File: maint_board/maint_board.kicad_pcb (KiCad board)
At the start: 2 copper layers, 151.1 x 90.1 mm, 96 parts, among them J1 USB_mini_micro_B, J2 4P4C, J3 TC2030-IDC_FB, K1 KEYSW, K10 KEYSW, K11 KEYSW, K12 KEYSW, K13 KEYSW, K15 KEYSW, K16 KEYSW, K17 KEYSW, K18 KEYSW, K19 KEYSW, K2 KEYSW, K20 KEYSW, K29 KEYSW, K3 KEYSW, K30 KEYSW, K31 KEYSW, K4 KEYSW, K5 KEYSW, K6 KEYSW, K8 KEYSW, K9 KEYSW, Q1 Q_NMOS_GSD, SW1 SW_PUSH, U1 ATMEGA32U4, X1 XTAL_GND

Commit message: commit before reinstall computer
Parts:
- removed G***: LOGO, grafic:qr
- removed G***: LOGO, grafic:loggo2
- removed REF**: OSHW-Logo2_7.3x6mm_SilkScreen, Symbol:OSHW-Logo2_7.3x6mm_SilkScreen
- removed REF** (x3): MountingHole_2.2mm_M2, MountingHole:MountingHole_2.2mm_M2
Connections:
- R1 pad 2: Net-(R1-Pad2) -> rst_prog
- SW1 pad 2: Net-(R1-Pad2) -> rst_prog
- U1 pad 12: rst_prog -> (no net)
- U1 pad 13: Net-(R1-Pad2) -> rst_prog
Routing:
- net rst_prog: track 18.9 -> 61.6 mm, vias 0 -> 1
- net Net-(R1-Pad2): track 41.1 -> 0.00 mm, vias 1 -> 0

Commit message: updated submodule
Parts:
- K1, K10, K11, K12, K13, K15, K16, K17, K18, K19, K2, K20, K29, K3, K30, K31, K4, K5, K6, K8, K9: footprint keyswitches:SW_MX_reversible -> switches:SW_MX_reversible
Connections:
- D41 pad 4: (no net) -> Net-(D41-Pad4)
- D42 pad 4: (no net) -> Net-(D42-Pad4)
- D43 pad 1: (no net) -> Net-(D43-Pad1)
- D43 pad 6: (no net) -> Net-(D43-Pad6)
- D44 pad 3: (no net) -> Net-(D44-Pad3)
- D44 pad 4: (no net) -> Net-(D44-Pad4)
- J1 pad 4: (no net) -> Net-(J1-Pad4)
- U1 pad 1: (no net) -> Net-(U1-Pad1)
- U1 pad 12: (no net) -> Net-(U1-Pad12)
- U1 pad 20: (no net) -> Net-(U1-Pad20)
- U1 pad 25: (no net) -> Net-(U1-Pad25)
- U1 pad 26: (no net) -> Net-(U1-Pad26)
- U1 pad 36: (no net) -> Net-(U1-Pad36)
- U1 pad 42: (no net) -> Net-(U1-Pad42)
- U1 pad 7: (no net) -> Net-(U1-Pad7)
- U1 pad 8: (no net) -> Net-(U1-Pad8)

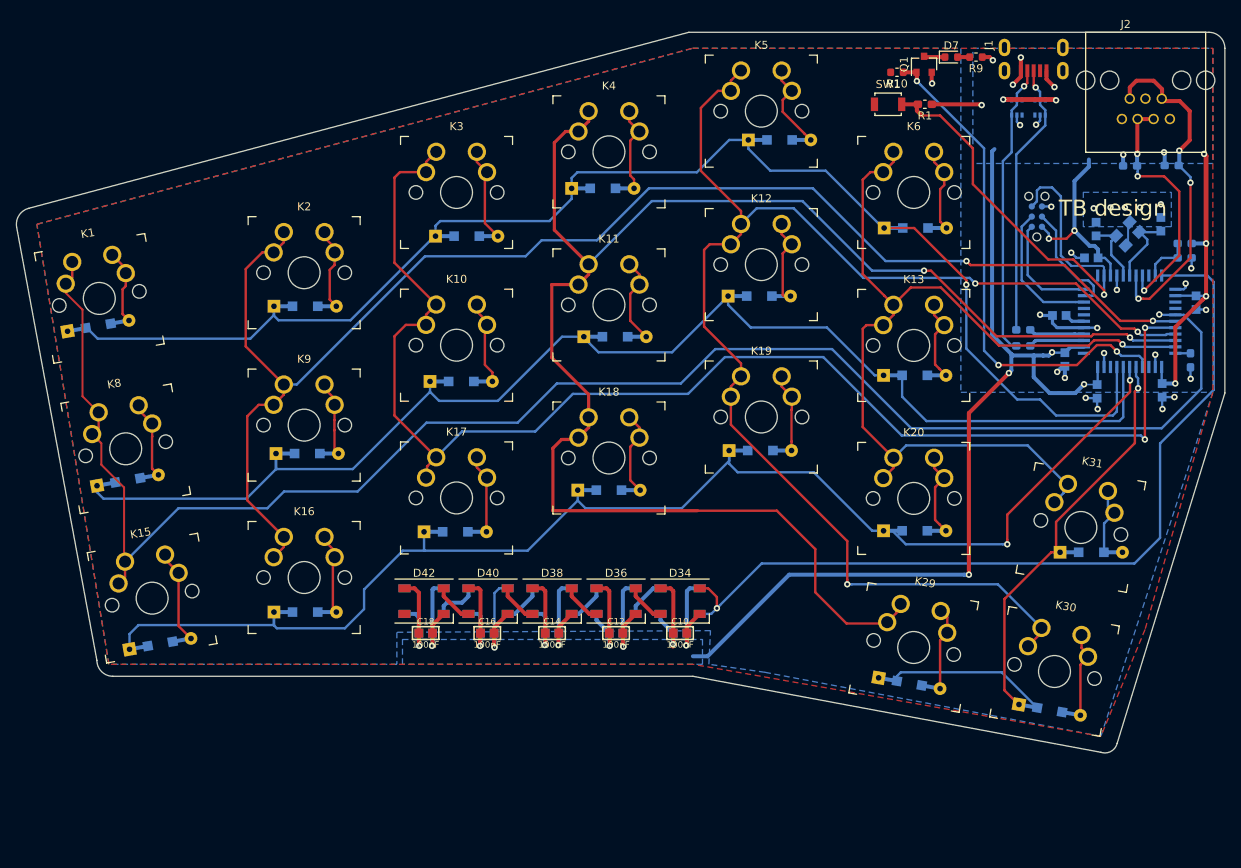
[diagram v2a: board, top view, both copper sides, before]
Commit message: removed two leds and fixed recet and usb port
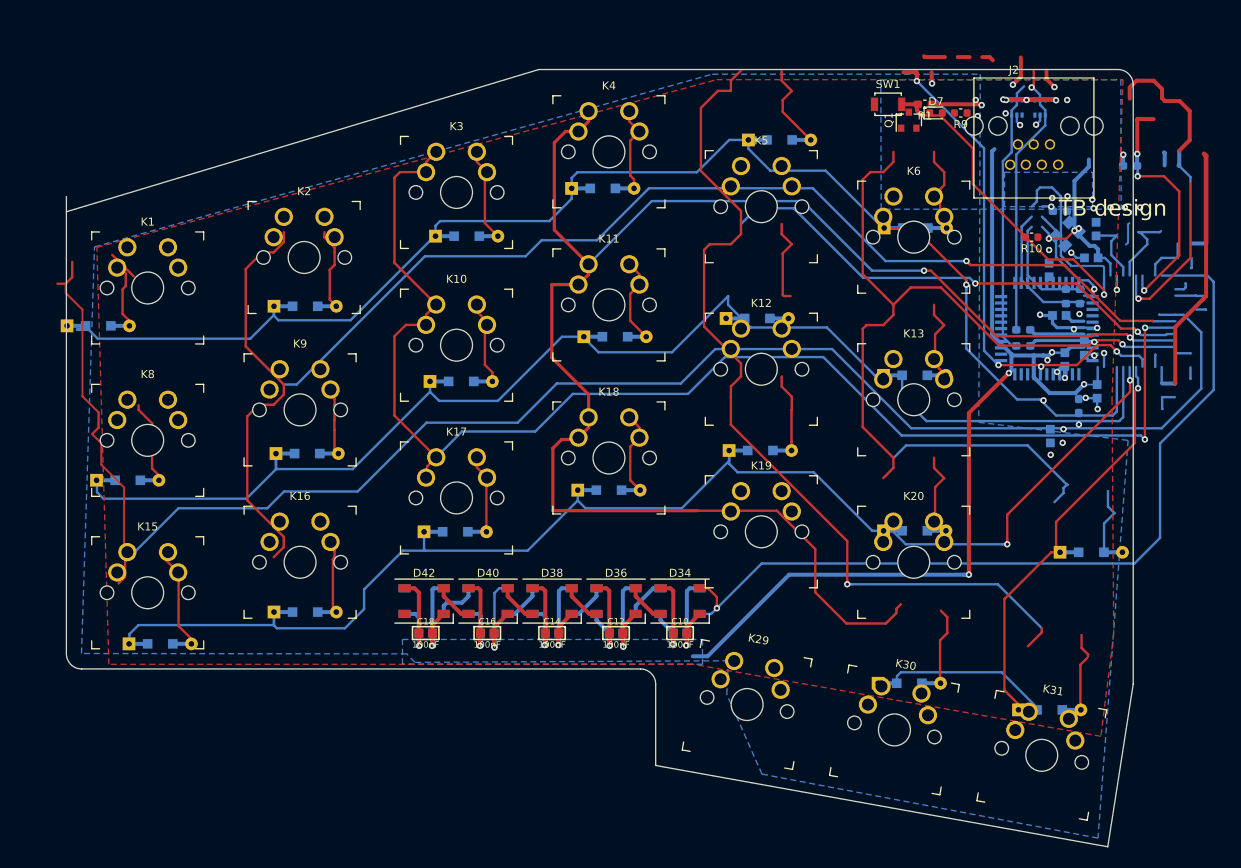
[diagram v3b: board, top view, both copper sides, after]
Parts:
- removed J1: USB_mini_micro_B, my_connectors:usb_minib_wm5462ct-nd
- removed J3: TC2030-IDC_FB, Connector:Tag-Connect_TC2030-IDC-NL_2x03_P1.27mm_Vertical
- moved K31 28.9 mm to (181.6, 119.4)
- moved R10 26.6 mm to (180.3, 54.6)
- moved K29 22.0 mm to (144.8, 113.0)
- moved K30 21.3 mm to (163.2, 116.2)
- moved C2 15.1 mm to (182.5, 58.7)
- moved C3 15.1 mm to (182.7, 79.5)
- moved C5 15.1 mm to (186.9, 68.5)
- moved J2 15.1 mm to (182.1, 40.7)
- moved R5 15.1 mm to (183.9, 51.4)
- moved R6 15.1 mm to (186.2, 75.7)
- moved R8 15.1 mm to (185.5, 61.1)
- moved R7 15.1 mm to (185.5, 62.9)
- moved K19 14.4 mm to (146.6, 91.4)
- moved K12 13.1 mm to (146.6, 71.1)
- moved K5 11.9 mm to (146.6, 50.8)
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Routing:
- net /keys/Col6: track 117.0 -> 27.4 mm
- net /keys/Col5: track 172.5 -> 262.1 mm, vias 3 -> 5
- net (no net): track 0.00 -> 50.8 mm
- net /keys/Col2: track 179.3 -> 128.5 mm
- net /mcu/usb_D-: track 36.7 -> 34.5 mm, vias 1 -> 0
- net GND: track 107.7 -> 109.1 mm, vias 31 -> 33
- net VCC: track 274.5 -> 273.2 mm
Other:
- board size 151.1 x 90.1 mm -> 133.3 x 97.2 mm

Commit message: this is before I switch to usb C
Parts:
- removed C13, C14, C15, C16, C17, C18: 100nF, keyboard_parts:C_1608
- removed D37, D38, D39, D40, D41, D42: SK6812, LED_SMD:LED_SK6812_PLCC4_5.0x5.0mm_P3.2mm
- added D14: 1N4148W, Diode_SMD:D_SOD-323, F.Cu at (170.2, 42.9)
- added H1: MountingHole, MountingHole:MountingHole_2.2mm_M2_ISO7380, F.Cu at (77.5, 52.1)
- added H2: MountingHole, MountingHole:MountingHole_2.2mm_M2_ISO7380, F.Cu at (154.9, 39.4)
- added H3: MountingHole, MountingHole:MountingHole_2.2mm_M2_ISO7380, F.Cu at (174.5, 105.9)
- added J1: USB_mini_micro_B, TB_connectors:usb_minib_wm5462ct-nd, F.Cu at (166.4, 36.8)
- added J3: TC2030-IDC_FB, Connector:Tag-Connect_TC2030-IDC-NL_2x03_P1.27mm_Vertical, B.Cu at (190.5, 83.2)
- added J4: Conn_01x04, Connector_PinHeader_1.00mm:PinHeader_1x04_P1.00mm_Vertical, F.Cu at (192.5, 41.9)
- added J5: USB_C_Receptacle_USB2.0, Connector_USB:USB_C_Receptacle_Palconn_UTC16-G, F.Cu at (146.6, 38.6)
- added JP1: SolderJumper_2_Open, Jumper:SolderJumper-2_P1.3mm_Open_RoundedPad1.0x1.5mm, F.Cu at (185.2, 54.6)
- added JP2: SolderJumper_2_Open, Jumper:SolderJumper-2_P1.3mm_Open_RoundedPad1.0x1.5mm, F.Cu at (182.4, 54.6)
- added JP3: SolderJumper_2_Open, Jumper:SolderJumper-2_P1.3mm_Open_RoundedPad1.0x1.5mm, F.Cu at (179.8, 54.6)
- added TP1: TestPoint_Flag, TestPoint:TestPoint_Pad_1.5x1.5mm, F.Cu at (191.0, 97.5)
- added TP2: TestPoint_Flag, TestPoint:TestPoint_Pad_1.5x1.5mm, F.Cu at (192.0, 48.5)
- D43, D44: moved to F.Cu
- J2: footprint my_connectors:glx-n-44_reverseble -> TB_connectors:glx-n-44_reverseble
- moved C11 61.9 mm to (190.3, 103.0), turned to 90 degrees
- moved C12 61.9 mm to (190.3, 103.0), turned to 90 degrees
- moved D35 58.0 mm to (186.3, 103.0), turned to 90 degrees
- moved D36 58.0 mm to (186.3, 103.0), turned to 90 degrees
- moved R9 57.9 mm to (176.3, 96.8)
- moved D7 56.6 mm to (176.3, 95.1), turned to 180 degrees
- moved C10 55.3 mm to (190.5, 92.6), turned to 90 degrees
- moved C9 55.3 mm to (190.5, 92.6), turned to 90 degrees
- moved Q1 53.8 mm to (177.0, 92.5), turned to 270 degrees
- moved D33 50.6 mm to (186.5, 92.6), turned to 90 degrees
- moved D34 50.6 mm to (186.5, 92.6), turned to 90 degrees
- moved R10 35.1 mm to (177.0, 89.5)
- moved SW1 34.3 mm to (192.3, 54.9), turned to 270 degrees
- moved R1 31.7 mm to (191.5, 58.2), turned to 0 degrees
- moved X1 27.3 mm to (184.7, 81.5), turned to 180 degrees
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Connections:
- U1 pad 18: /mcu/SCL -> i2c_scl
- U1 pad 19: /mcu/SDA -> i2c_sda
- U1 pad 20: Net-(U1-Pad20) -> serial
- U1 pad 36: Net-(U1-Pad36) -> /keys/Row1
- U1 pad 41: /keys/Row1 -> Net-(U1-Pad41)
- U1 pad 7: Net-(U1-Pad7) -> /mcu/Vbus
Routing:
- net VCC: track 273.2 -> 61.8 mm, vias 23 -> 9
- net /keys/Col5: track 262.1 -> 139.8 mm, vias 5 -> 2
- net /keys/Col6: track 27.4 -> 124.9 mm, vias 1 -> 2
- net /Leds/Din: track 107.1 -> 26.7 mm, vias 1 -> 2
- net (no net): track 50.8 -> 0.35 mm
- net /mcu/Vbus: track 0.00 -> 50.2 mm, vias 0 -> 3
- net /keys/Col1: track 210.2 -> 167.2 mm, vias 1 -> 0
- net i2c_sda: track 0.00 -> 40.0 mm, vias 0 -> 2
- net /keys/Col3: track 169.1 -> 129.8 mm, vias 2 -> 0
- net i2c_scl: track 0.00 -> 38.1 mm, vias 0 -> 2
- net /keys/Col4: track 201.0 -> 168.2 mm
- net serial: track 0.00 -> 32.2 mm, vias 0 -> 3
- net Net-(Q1-Pad1): track 63.1 -> 31.8 mm, vias 3 -> 1
- net /keys/Row1: track 177.8 -> 148.4 mm, vias 1 -> 2
- net /mcu/SCL: track 42.6 -> 14.2 mm, vias 3 -> 1
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- added copper zone on F.Cu, net VCC
- removed copper zone on F.Cu, net GND
- removed copper zone on B.Cu, net VCC
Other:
- board size 133.3 x 97.2 mm -> 134.6 x 97.8 mm
- net class Min: clearance 0.1 -> 0.2; trace_width 0.1 -> 0.2
- rule trace_min: 0.1 -> 0.2
- board text added: "toddis_kb revB"

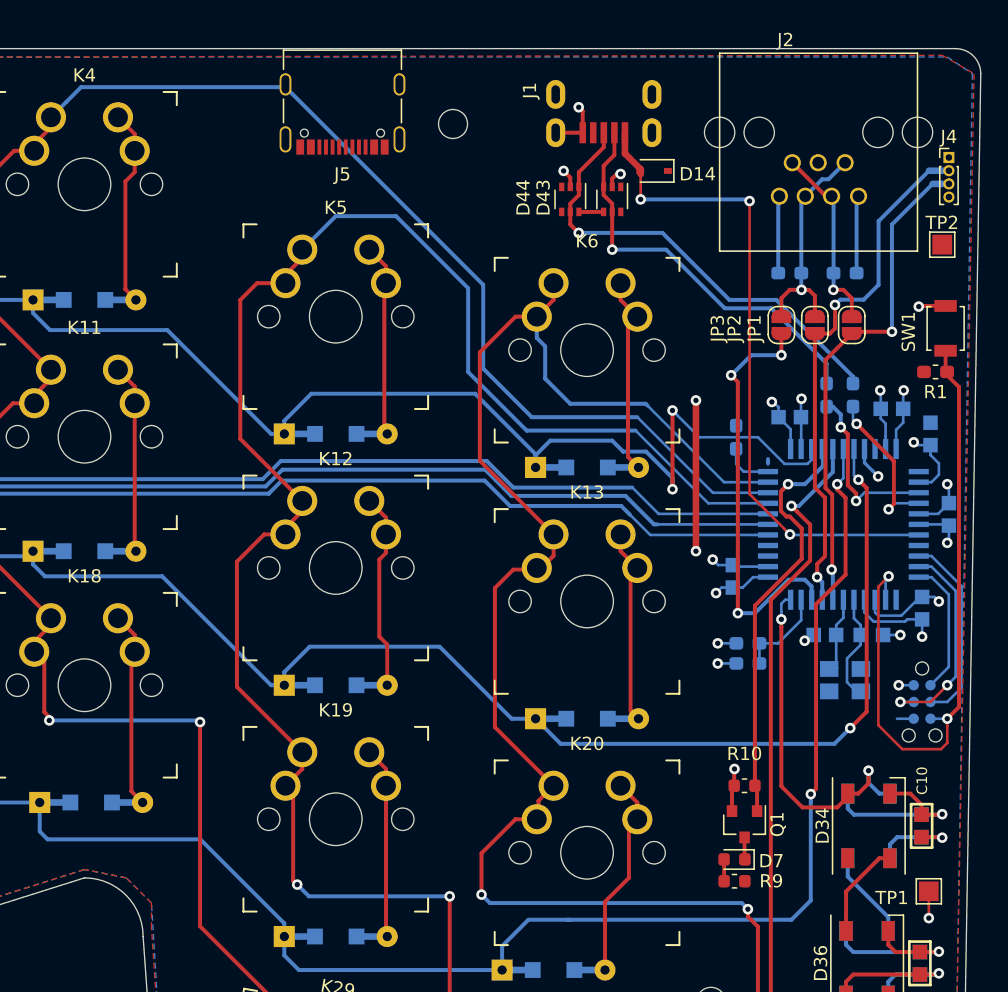
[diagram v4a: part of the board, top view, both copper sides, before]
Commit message: added filter on usb shield
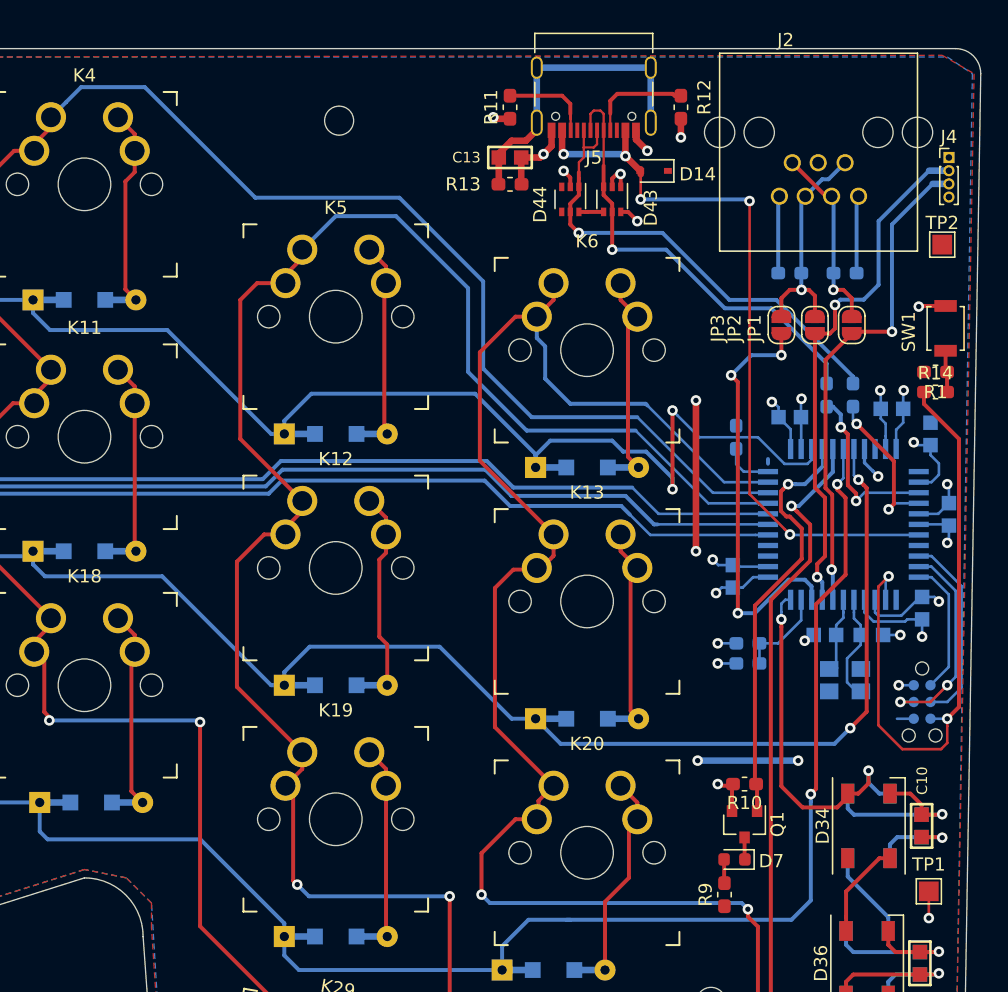
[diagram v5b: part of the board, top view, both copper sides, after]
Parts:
- removed J1: USB_mini_micro_B, TB_connectors:usb_minib_wm5462ct-nd
- added C13: 4n7, keyboard_parts:C_1608, F.Cu at (159.3, 41.9)
- added R11: 5k1, Resistor_SMD:R_0603_1608Metric_Pad1.05x0.95mm_HandSolder, F.Cu at (159.3, 38.1)
- added R12: 5k1, Resistor_SMD:R_0603_1608Metric_Pad1.05x0.95mm_HandSolder, F.Cu at (172.2, 38.1)
- added R13: 1M, Resistor_SMD:R_0603_1608Metric_Pad1.05x0.95mm_HandSolder, F.Cu at (159.3, 43.9)
- added R14: 330, Resistor_SMD:R_0603_1608Metric_Pad1.05x0.95mm_HandSolder, F.Cu at (191.5, 59.7)
- R10, R9: footprint Resistor_SMD:R_0603_1608Metric -> Resistor_SMD:R_0603_1608Metric_Pad1.05x0.95mm_HandSolder
- TP1: value TestPoint_Flag -> gnd
- TP2: value TestPoint_Flag -> Vcc
- moved J5 19.1 mm to (165.6, 37.3)
- moved H2 8.64 mm to (146.3, 39.1)
- moved R9 1.27 mm to (175.5, 97.8), turned to 90 degrees
- moved R10 0.13 mm to (177.0, 89.4)
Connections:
- D14 pad 2: /mcu/Vbus -> vbus
- D43 pad 1: Net-(D43-Pad1) -> GND
- D43 pad 6: Net-(D43-Pad6) -> VCC
- J5 pad A1: Net-(J5-PadA1) -> GND
- J5 pad A12: Net-(J5-PadA1) -> GND
- J5 pad A4: Net-(J5-PadA4) -> vbus
- J5 pad A6: Net-(J5-PadA6) -> /mcu/usb_D+
- J5 pad A7: Net-(J5-PadA7) -> /mcu/usb_D-
- J5 pad A9: Net-(J5-PadA4) -> vbus
- J5 pad B1: Net-(J5-PadA1) -> GND
- J5 pad B12: Net-(J5-PadA1) -> GND
- J5 pad B4: Net-(J5-PadA4) -> vbus
- J5 pad B6: Net-(J5-PadB6) -> /mcu/usb_D+
- J5 pad B7: Net-(J5-PadB7) -> /mcu/usb_D-
- J5 pad B9: Net-(J5-PadA4) -> vbus
- R1 pad 2: rst_prog -> Net-(R1-Pad2)
- SW1 pad 2: rst_prog -> Net-(R1-Pad2)
- U1 pad 7: /mcu/Vbus -> vbus
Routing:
- net vbus: track 0.00 -> 57.1 mm, vias 0 -> 5
- net /mcu/Vbus: track 50.2 -> 0.00 mm, vias 3 -> 0
- net Net-(C13-Pad2): track 0.00 -> 24.3 mm
- net VCC: track 61.8 -> 71.0 mm, vias 9 -> 12
- net Net-(J5-PadA5): track 0.00 -> 7.87 mm
- net GND: track 81.6 -> 89.0 mm, vias 18 -> 21
- net Net-(J5-PadB5): track 0.00 -> 7.22 mm
- net /mcu/usb_D-: track 30.8 -> 34.4 mm
- net Net-(R1-Pad2): track 0.00 -> 3.32 mm
- net rst_prog: track 51.5 -> 49.0 mm
- net /mcu/usb_D+: track 34.7 -> 36.5 mm
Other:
- rule trace_min: 0.2 -> 0.175

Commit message: added som libes
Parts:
- added G***: LOGO, loggo:qr_500_500, F.Cu at (182.4, 65.3)
- added G***: LOGO, loggo:loggo_1200_1200, F.Cu at (183.9, 82.5)
- added REF**: OSHW-Logo2_7.3x6mm_SilkScreen, Symbol:OSHW-Logo2_7.3x6mm_SilkScreen, F.Cu at (140.0, 39.1)
